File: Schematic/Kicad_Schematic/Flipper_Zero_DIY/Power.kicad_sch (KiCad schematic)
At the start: 81 parts, among them x10 Connector 3P

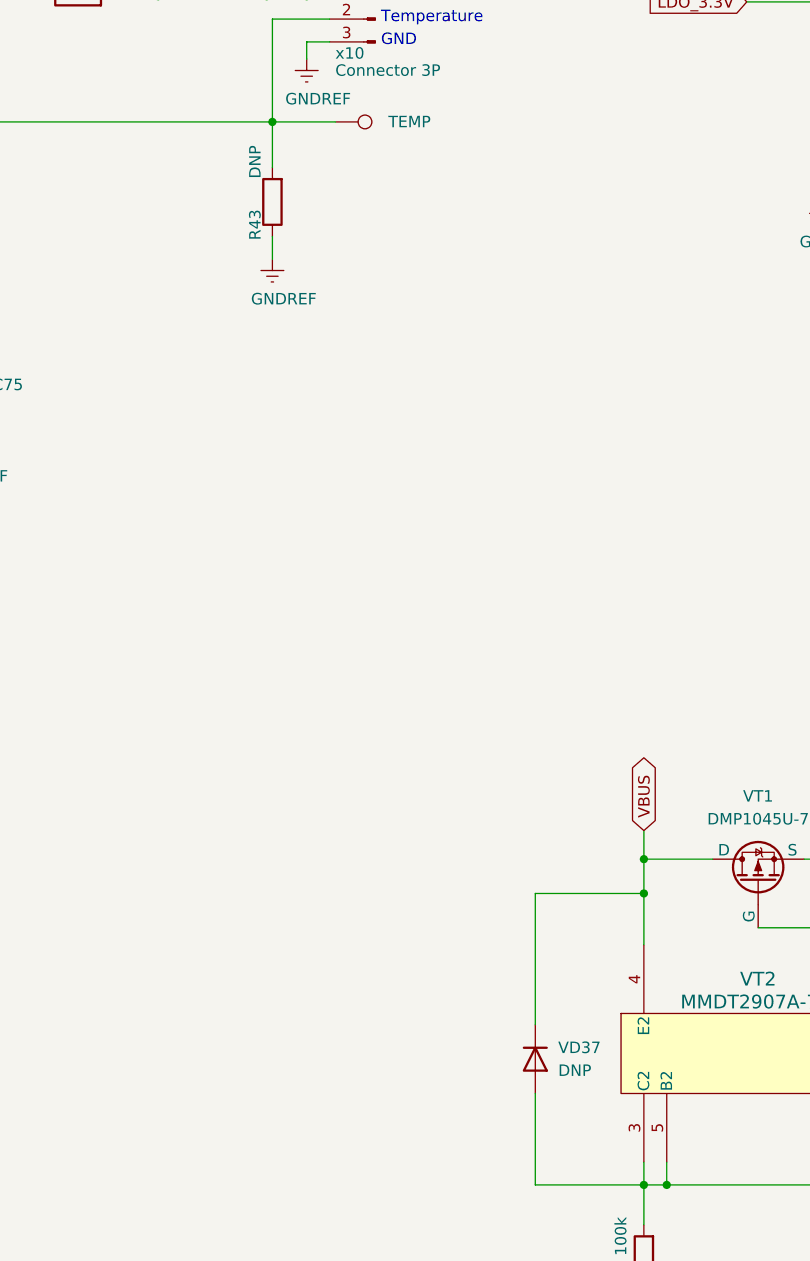
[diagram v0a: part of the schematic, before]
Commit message: finished MCU schematic & new design of front shematic
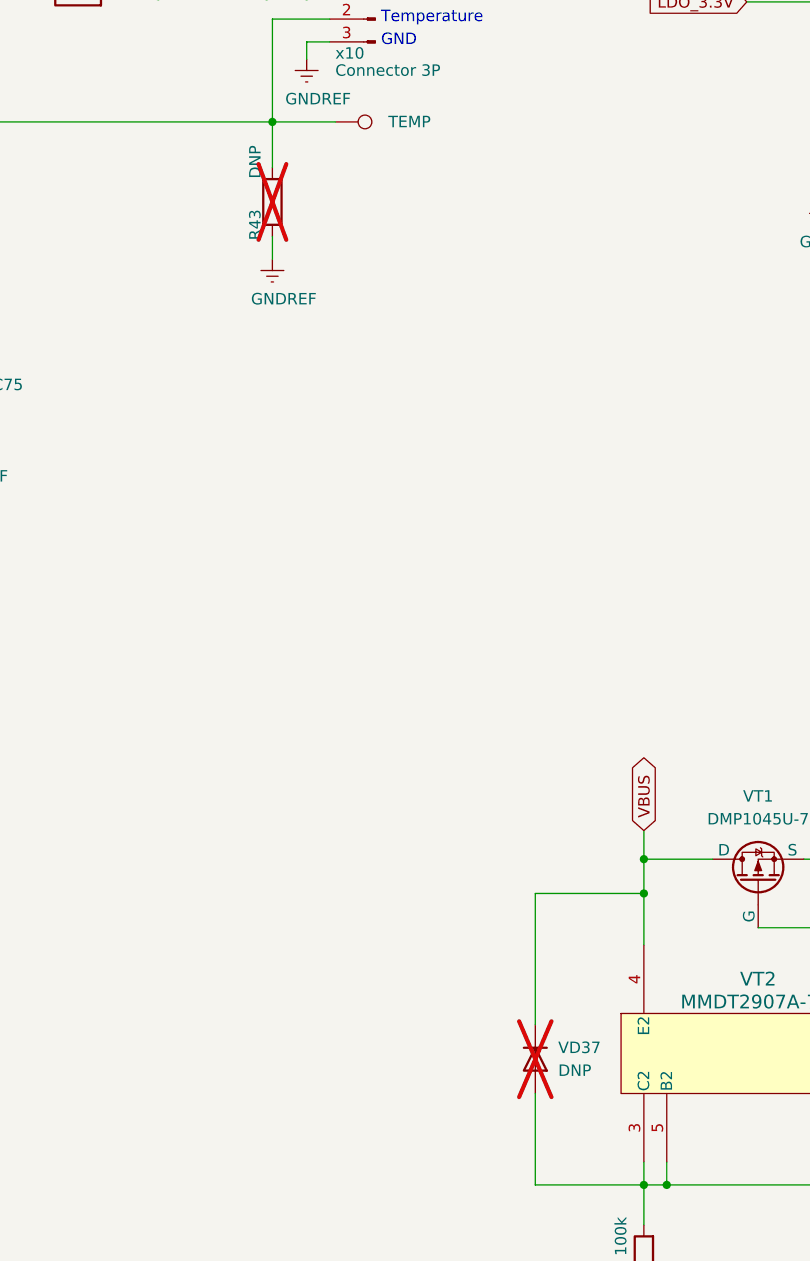
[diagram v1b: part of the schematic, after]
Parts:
- R43, VD37: now not fitted
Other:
- company: (none) -> Flipper Devices Inc.
- title: (none) -> Flipper Device DIY
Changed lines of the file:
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@@
 (kicad_sch (version 20230121) (generator eeschema)
   (paper "A3")
+  (title_block
+    (title "Flipper Device DIY")
+    (rev "13.F7B9C6")
+    (company "Flipper Devices Inc.")
+  )
   (junction (at 219.075 227.33) (diameter 0) (color 0 0 0 0)
   )
@@
   )
   (symbol (lib_id "Device:R") (at 312.42 110.49 180) (unit 1)
-    (in_bom yes) (on_board yes) (dnp no)
+    (in_bom yes) (on_board yes) (dnp yes)
     (property "Reference" "R43" (at 310.515 113.03 90)
       (effects (font (size 1.27 1.27)))
@@
   )
   (symbol (lib_id "Device:D") (at 341.63 205.74 270) (unit 1)
-    (in_bom yes) (on_board yes) (dnp no) (fields_autoplaced)
+    (in_bom yes) (on_board yes) (dnp yes) (fields_autoplaced)
     (property "Reference" "VD37" (at 344.17 204.47 90)
       (effects (font (size 1.27 1.27)) (justify left))

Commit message: finished Su-1-GHz-CC1101
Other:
- company: Flipper Devices Inc. -> Originally from : Flipper Devices Inc.
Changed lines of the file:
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@@
     (title "Flipper Device DIY")
     (rev "13.F7B9C6")
-    (company "Flipper Devices Inc.")
+    (company "Originally from : Flipper Devices Inc.")
+    (comment 1 "DIY Version 1.0")
   )
   (junction (at 219.075 227.33) (diameter 0) (color 0 0 0 0)

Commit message: added all changes to the changelog
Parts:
- x10: footprint Connector_PinHeader_2.00mm:PinHeader_1x03_P2.00mm_Horizontal -> Connector_PinHeader_2.54mm:PinHeader_1x03_P2.54mm_Horizontal
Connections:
- net GNDREF: now also DD6.17 (PGND), DD6.18 (PGND), DD6.25 (PAD)
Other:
- note added: "LiPo Charger"
- note added: "PNP Current Mirror"
- note added: "Testingpoints"
- note added: "Voltage Regulators"
- moved on the sheet: C65
